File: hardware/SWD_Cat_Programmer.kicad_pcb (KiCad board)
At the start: 2 copper layers, 40.5 x 20.1 mm, 27 parts, among them J1 DEBUG_OUT, P1 USB_C_Plug_USB2.0, U1 CH552G, U2 HX9193-33GB

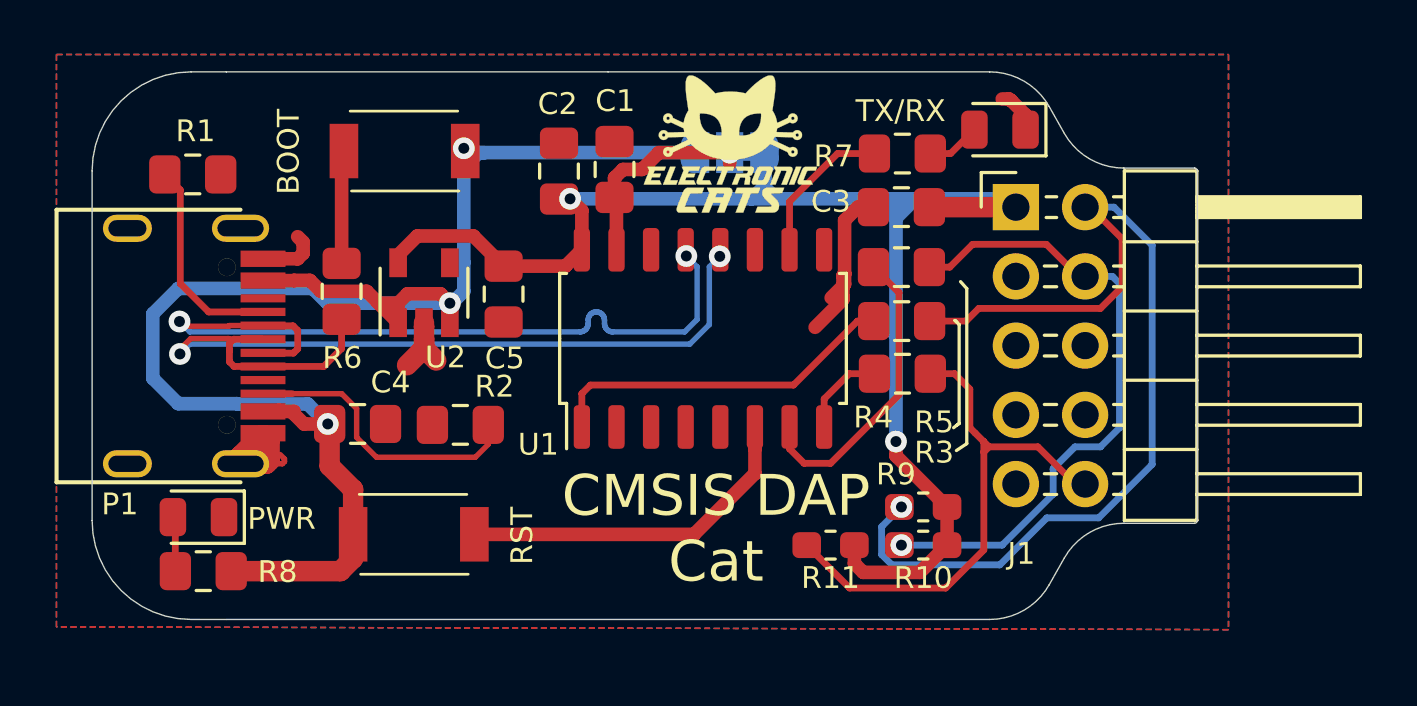
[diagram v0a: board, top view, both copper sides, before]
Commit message: pin output changed
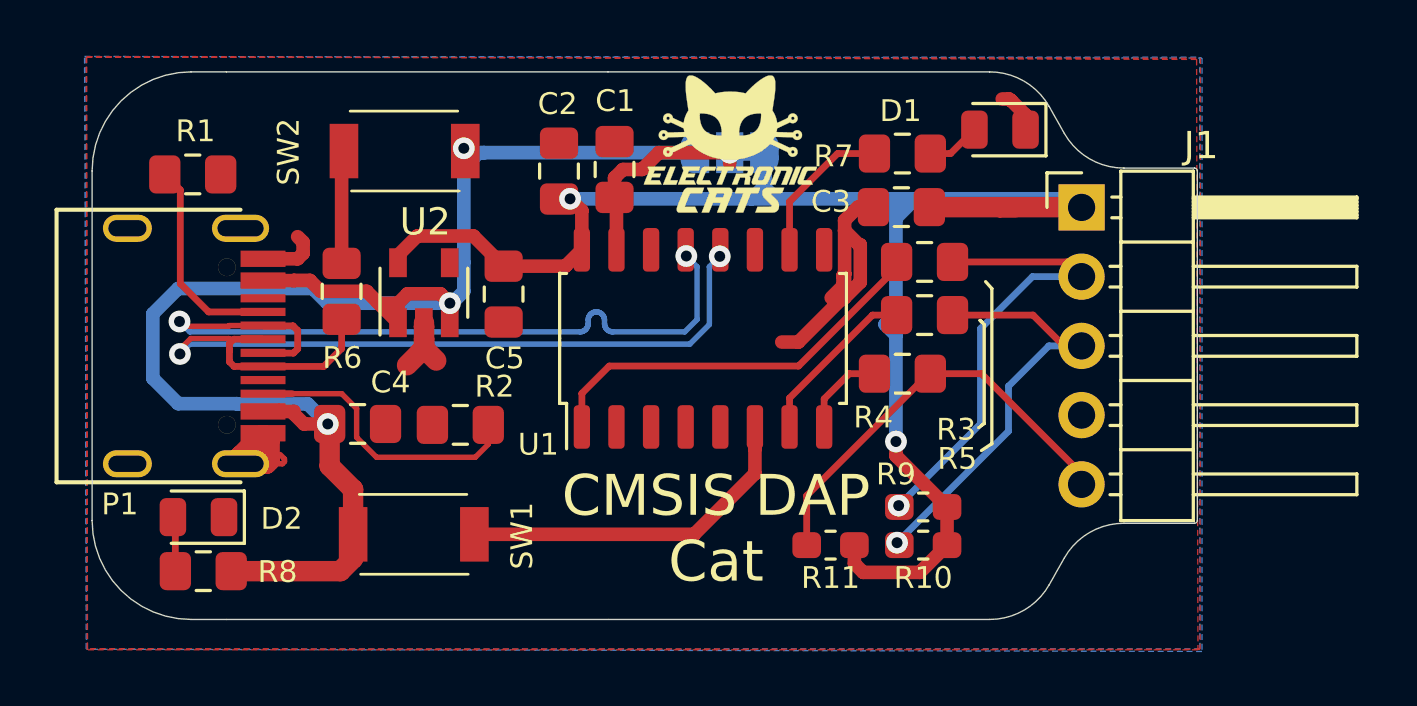
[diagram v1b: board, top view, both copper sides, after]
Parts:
- J1: value DEBUG_OUT -> DEBUG_OUTPUT; footprint Connector_PinHeader_2.54mm:PinHeader_2x05_P2.54mm_Horizontal -> Connector_PinHeader_2.54mm:PinHeader_1x05_P2.54mm_Horizontal
- U2: value HX9193-33GB -> AP2112K-3.3
- moved J1 2.41 mm to (167.6, 67.6)
- moved R5 2.33 mm to (161.8, 69.6)
- moved R3 1.95 mm to (161.8, 71.6)
- renumbered TX/RX to D1, PWR to D2, RST to SW1, BOOT to SW2
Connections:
- J1 pad 3: GND -> /SWCLK
- J1 pad 4: /SWCLK -> GND
- J1 pad 5: GND -> /RESET
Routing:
- net /SWDIO: track 35.9 -> 17.2 mm
- net /SWCLK: track 24.0 -> 15.9 mm
- net +3V3: track 53.6 -> 59.0 mm
- net Net-(R3-Pad2): track 11.7 -> 6.25 mm
- net /RESET: track 21.0 -> 16.1 mm
- net GND: track 19.6 -> 24.2 mm
- net Net-(R5-Pad2): track 13.0 -> 14.9 mm

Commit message: update label
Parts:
- renumbered SW2 to BOOT, SW1 to RST
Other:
- board text added: "CMSIS DAP Cat v1.1"
- board text removed: "CMSIS DAP Cat v1.0"
- board text removed: "NC"

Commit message: v1.1 align
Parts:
- moved R11 3.54 mm to (161.8, 81.0), turned to 180 degrees
- moved C3 0.85 mm to (161.8, 67.6)
- moved R4 0.81 mm to (161.8, 73.7)
- moved R7 0.81 mm to (161.8, 65.6)
- moved D1 0.59 mm to (165.0, 65.2), turned to 270 degrees
- moved R9 0.49 mm to (161.8, 78.1), turned to 180 degrees
- moved R10 0.43 mm to (161.8, 79.6), turned to 180 degrees
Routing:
- net +3V3: track 59.0 -> 57.1 mm
- net GND: track 24.2 -> 22.5 mm
- net Net-(R5-Pad2): track 14.9 -> 16.3 mm
- net /RESET: track 16.1 -> 15.1 mm
- net /LED: track 5.61 -> 6.61 mm
- net Net-(R3-Pad2): track 6.25 -> 7.12 mm
- net Net-(R4-Pad2): track 3.26 -> 3.88 mm
- net /SWCLK: track 15.9 -> 16.5 mm
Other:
- board text added: "DAP Cat v1.1"
- board text removed: "CMSIS DAP Cat"
- board text removed: "CMSIS DAP Cat v1.1"

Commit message: Update labels for Serial Adapter
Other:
- board text added: "RST/RX"
- board text added: "SWC/TX"

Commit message: abierto open hardware month edition
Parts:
- added G***: LOGO, Aesthetics:abierto, B.Cu at (143.7, 77.2)
- moved G*** 6.07 mm to (155.3, 77.0)
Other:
- board text added: "DAP Cat v1.2"
- board text added: "Open Hardware Month Edition"
- board text removed: "DAP Cat v1.1"

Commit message: Cupper Zones Fixed
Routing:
- net +5V: track 59.6 -> 45.2 mm
- removed copper zone on B.Cu, net (none)
- removed copper zone on F.Cu, net (none)

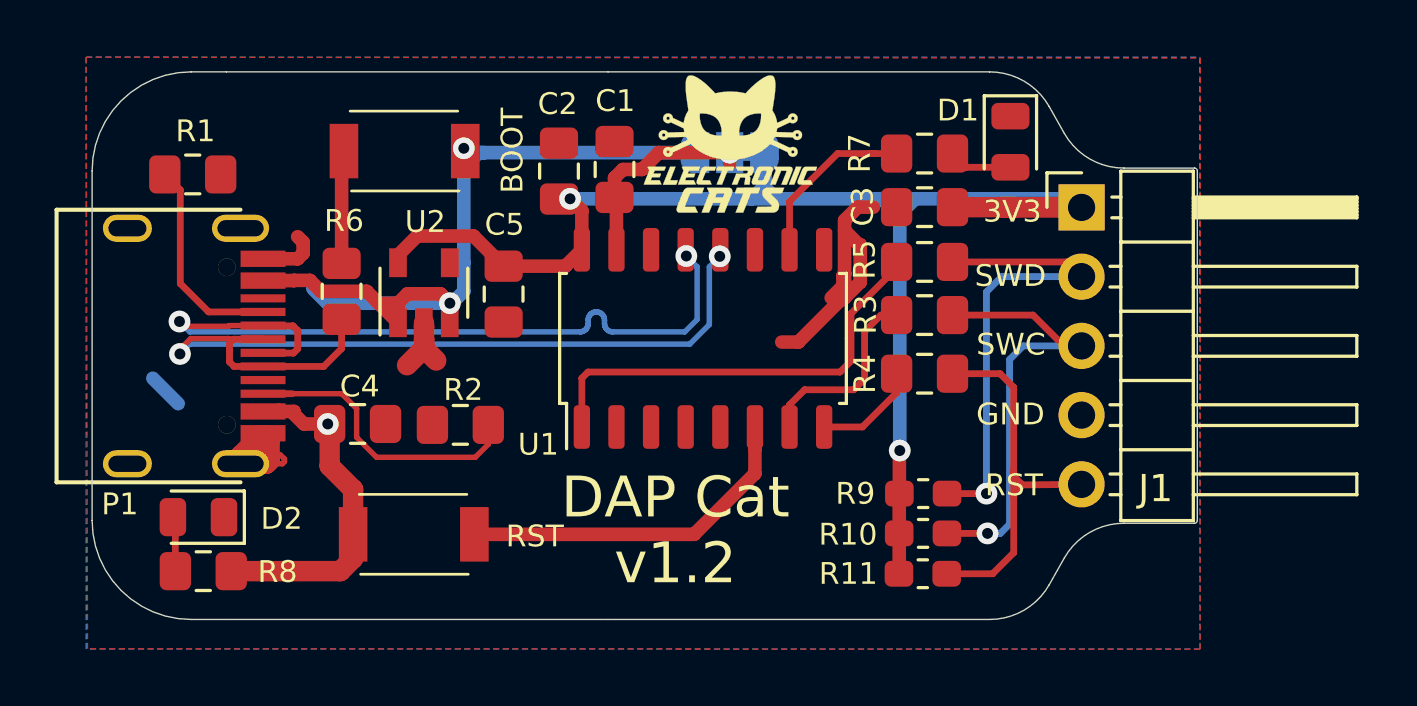
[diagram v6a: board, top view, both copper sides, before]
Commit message: enhanced routing
Signed-off-by: Ricardo Mena C <rgacort12@gmail.com>
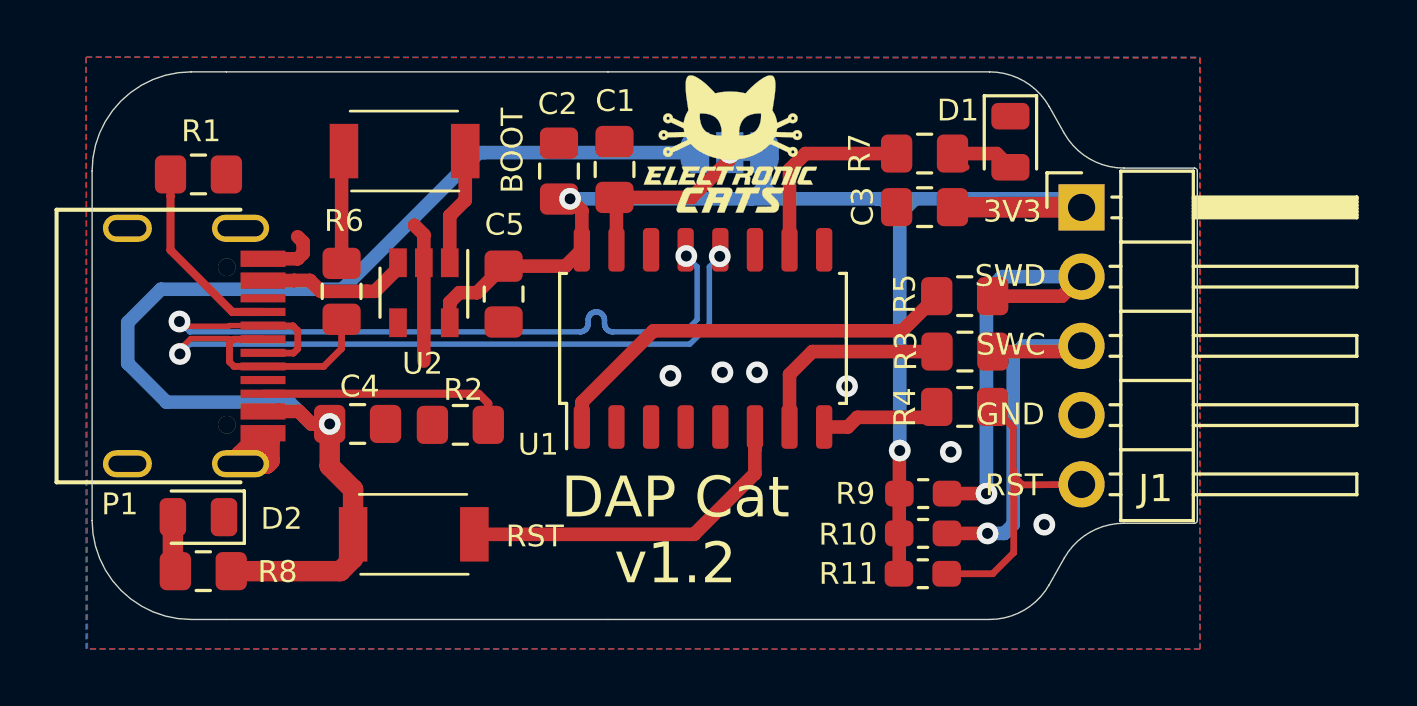
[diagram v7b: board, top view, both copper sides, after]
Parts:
- moved R3 2.00 mm to (163.3, 72.9)
- moved R5 1.94 mm to (163.3, 70.9)
- moved R4 1.91 mm to (163.3, 74.9)
- moved R1 0.21 mm to (135.2, 66.4)
- turned U2 to 270 degrees
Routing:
- net +5V: track 45.2 -> 56.4 mm, vias 3 -> 1
- net GND: track 22.5 -> 11.5 mm, vias 0 -> 6
- net +3V3: track 57.1 -> 53.1 mm
- net /RESET: track 15.1 -> 12.2 mm
- net /SWCLK: track 16.5 -> 14.8 mm
- net Net-(P1-PadB5): track 10.8 -> 9.20 mm
- net /SWDIO: track 17.5 -> 16.1 mm
- net Net-(R5-Pad2): track 16.3 -> 15.5 mm
- net Net-(D1-Pad2): track 2.33 -> 3.05 mm
- net Net-(C1-Pad1): track 7.72 -> 7.05 mm
- net Net-(P1-PadA5): track 7.71 -> 7.11 mm
- net Net-(R3-Pad2): track 7.12 -> 7.69 mm
- net Net-(R4-Pad2): track 3.88 -> 4.44 mm
- net /LED: track 6.61 -> 7.12 mm

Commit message: Fix labels, added contribution name Ricardo Mena
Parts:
- renumbered D2 to ON, D1 to TX
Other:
- board text added: "DAP Cat v1.3"
- board text removed: "DAP Cat v1.2"
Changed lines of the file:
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@@
-(kicad_pcb (version 20171130) (host pcbnew 5.0.2+dfsg1-1)
+(kicad_pcb (version 20171130) (host pcbnew "(5.1.6-0-10_14)")
   (general
     (thickness 1.6)
@@
     (rev 1.0)
     (company "Electronic Cats")
+    (comment 1 "Ricardo Mena C rgacort12@gmail.com")
     (comment 2 "Felipe Islas")
     (comment 3 "Eduaro Wero")
@@
   )
   (setup
-    (last_trace_width 0.5)
+    (last_trace_width 0.25)
     (user_trace_width 0.2)
     (user_trace_width 0.3)
@@
     (zone_45_only no)
     (trace_min 0.2)
-    (segment_width 0.2)
-    (edge_width 0.05)
     (via_size 0.8)
     (via_drill 0.4)
@@
     (uvia_min_size 0.2)
     (uvia_min_drill 0.1)
+    (edge_width 0.05)
+    (segment_width 0.2)
     (pcb_text_width 0.3)
     (pcb_text_size 1.5 1.5)
@@
     (tags diode)
     (attr smd)
-    (fp_text reference D2 (at -3.05072 -0.05632) (layer F.SilkS)
+    (fp_text reference ON (at -3.05072 -0.05632) (layer F.SilkS)
       (effects (font (size 0.8 0.8) (thickness 0.12)))
     )
@@
     (tags diode)
     (attr smd)
-    (fp_text reference D1 (at -1.15 1.925 180) (layer F.SilkS)
+    (fp_text reference TX (at -1.15 1.925 180) (layer F.SilkS)
       (effects (font (size 0.8 0.8) (thickness 0.12)))
     )
@@
     (effects (font (size 1 1) (thickness 0.25)) (justify mirror))
   )
-  (gr_text "DAP Cat\nv1.2" (at 152.71 79.46) (layer F.SilkS)
+  (gr_text "DAP Cat\nv1.3" (at 152.71 79.46) (layer F.SilkS)
     (effects (font (size 1.5 1.5) (thickness 0.3)))
   )
@@
     (effects (font (size 1 1) (thickness 0.25)) (justify mirror))
   )
-  (gr_text "DAP Cat\nv1.2" (at 144.58 65.59) (layer B.SilkS)
+  (gr_text "DAP Cat\nv1.3" (at 144.58 65.59) (layer B.SilkS)
     (effects (font (size 1.5 1.5) (thickness 0.3)) (justify mirror))
   )
